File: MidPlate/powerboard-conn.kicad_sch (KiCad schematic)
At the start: 10 parts, among them J3 Molex Microfit 3.0

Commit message: update to midplate
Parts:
- removed J3 (x2): Molex Microfit 3.0, bots:Molex_Micro-Fit_3.0_43650-0215_1x02_P3.00mm_Vertical, symbol bots:Molex_Microfit_3.0_1x2
- added J4, J5: Molex MicroFit 1x2_SMD, bots:Molex_Micro-Fit_3.0_43650-0224_1x02-1MP_P3.00mm_Vertical, symbol bots:Molex_Microfit_3.0_1x2_SMD
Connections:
- net CHICKER: now also J4.2 (Pin_2)
- net EXTRA: now also J5.2 (Pin_2)
- net HV: now also J4.1 (Pin_1), J5.1 (Pin_1)

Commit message: midplate mods
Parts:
- removed H1: VCC_PB, bots:MountingHole_2.7mm_M2.5_DIN965_Pad, symbol Mechanical:MountingHole_Pad
- removed H2: GND_PB, bots:MountingHole_2.7mm_M2.5_DIN965_Pad, symbol Mechanical:MountingHole_Pad
- removed H3: CANL_PB, bots:MountingHole_2.7mm_M2.5_DIN965_Pad, symbol Mechanical:MountingHole_Pad
- removed H4: CANH_PB, bots:MountingHole_2.7mm_M2.5_DIN965_Pad, symbol Mechanical:MountingHole_Pad
- removed H5: NC, bots:MountingHole_2.7mm_M2.5_DIN965_Pad, symbol Mechanical:MountingHole_Pad
- removed H6: EXTRA, bots:MountingHole_2.7mm_M2.5_DIN965_Pad, symbol Mechanical:MountingHole_Pad
- removed H7: HV, bots:MountingHole_2.7mm_M2.5_DIN965_Pad, symbol Mechanical:MountingHole_Pad
- removed H8: CHICKER, bots:MountingHole_2.7mm_M2.5_DIN965_Pad, symbol Mechanical:MountingHole_Pad
- added H1: VCC_PB, bots:Keystone_24929, symbol bots:ZeroH_Keystone24929_Pad
- added H2: GND_PB, bots:Keystone_24929, symbol bots:ZeroH_Keystone24929_Pad
- added H3: CANL_PB, bots:Keystone_24929, symbol bots:ZeroH_Keystone24929_Pad
- added H4: CANH_PB, bots:Keystone_24929, symbol bots:ZeroH_Keystone24929_Pad
- added H5: NC, bots:Keystone_24929, symbol bots:ZeroH_Keystone24929_Pad
- added H6: EXTRA, bots:Keystone_24929, symbol bots:ZeroH_Keystone24929_Pad
- added H7: HV, bots:Keystone_24929, symbol bots:ZeroH_Keystone24929_Pad
- added H8: CHICKER, bots:Keystone_24929, symbol bots:ZeroH_Keystone24929_Pad
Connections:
- net CHICKER: now also H8.1
- net EXTRA: now also H6.1
- net GND: now also H2.1
- net HV: now also H7.1
- net VCC: now also H1.1
- new net CAN+: H4.1
- new net CAN-: H3.1
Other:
- moved on the sheet: J4, J5

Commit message: midplate changes, ready for order
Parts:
- added J13: JST_BM04B-GHS-TBT, bots:JST_BM04B-GHS-TBT, symbol bots:JST_BM04B-GHS-TBT
- added R4, R5: R_0OHM_JUMPER, bots:R_0603_1608Metric, symbol bots:R_0OHM_JUMPER
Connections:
- net CAN+: now also J13.3, R4.1; no longer H4.1
- net CAN-: now also J13.2, R5.2; no longer H3.1
- net GND: now also J13.1, J13.4
- new net CANR+: H4.1, R4.2
- new net CANR-: H3.1, R5.1
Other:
- moved on the sheet: H3, H4

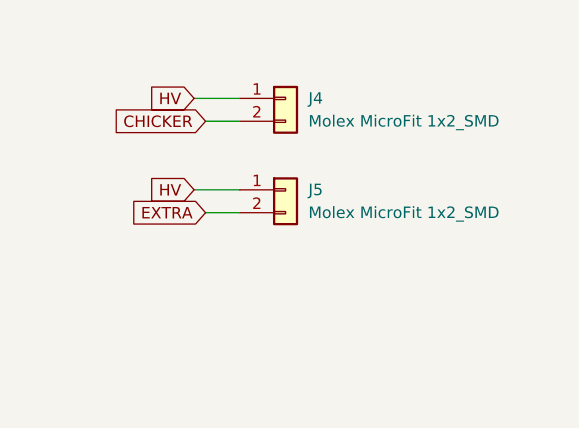
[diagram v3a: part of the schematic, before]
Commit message: midplate updates
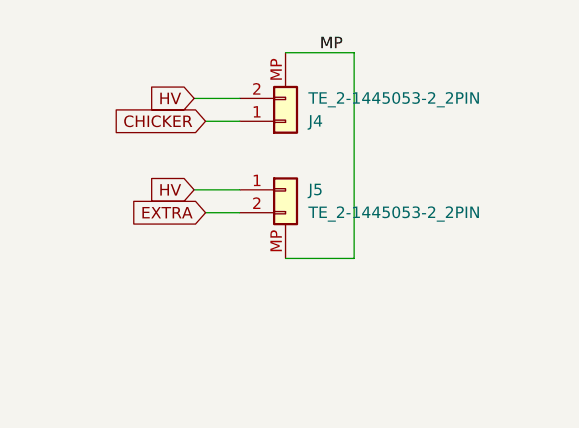
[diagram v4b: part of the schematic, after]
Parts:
- removed J4, J5: Molex MicroFit 1x2_SMD, bots:Molex_Micro-Fit_3.0_43650-0224_1x02-1MP_P3.00mm_Vertical, symbol bots:Molex_Microfit_3.0_1x2_SMD
- added J4, J5: TE_2-1445053-2_2PIN, bots:TE_2-1445053-2_2PIN, symbol bots:TE_2-1445053-2_2PIN
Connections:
- net CHICKER: now also J4.1 (Pin_1)
- net EXTRA: now also J5.2 (Pin_2)
- net HV: now also J4.2 (Pin_2), J5.1 (Pin_1)
- new net MP: J4.MP, J4.MP1, J5.MP, J5.MP1

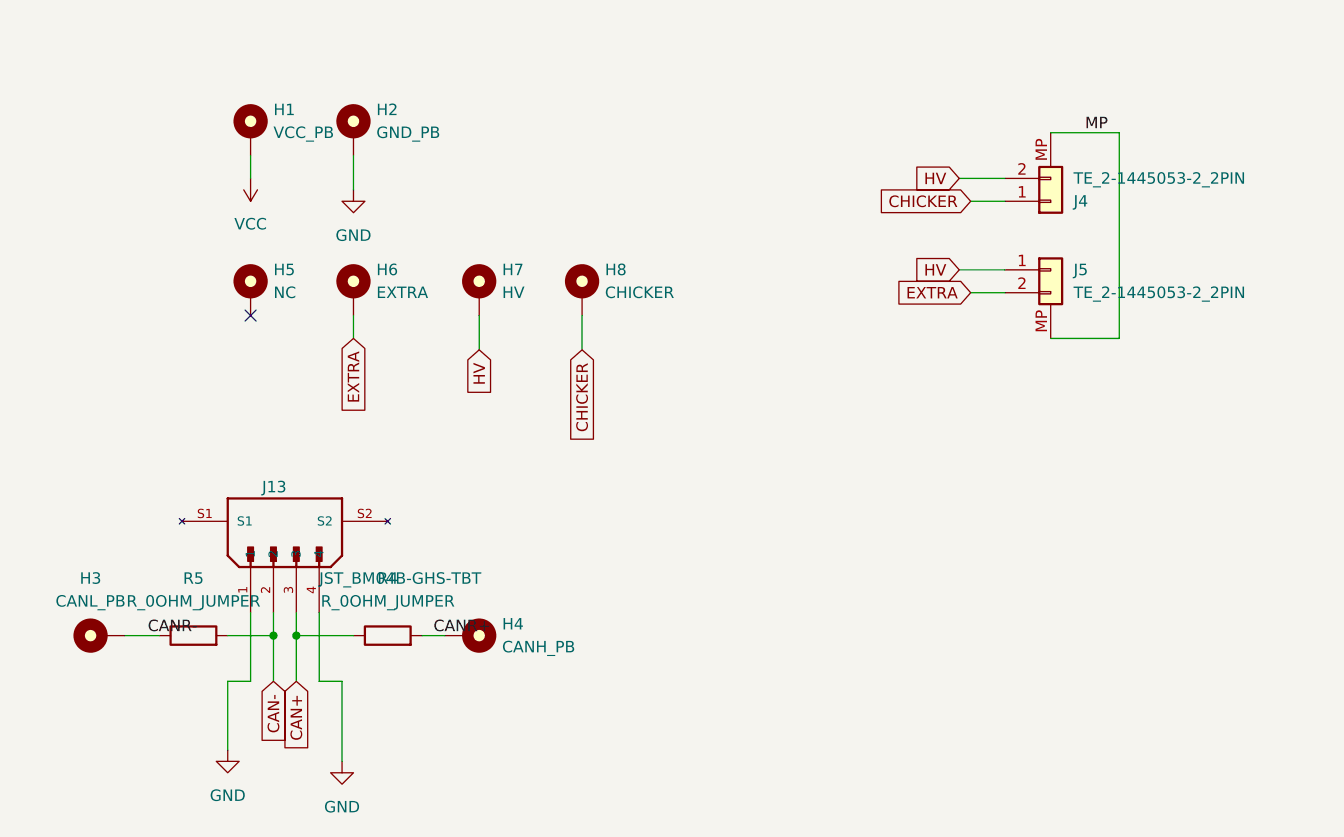
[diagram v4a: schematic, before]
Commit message: midplate 5V buck converter
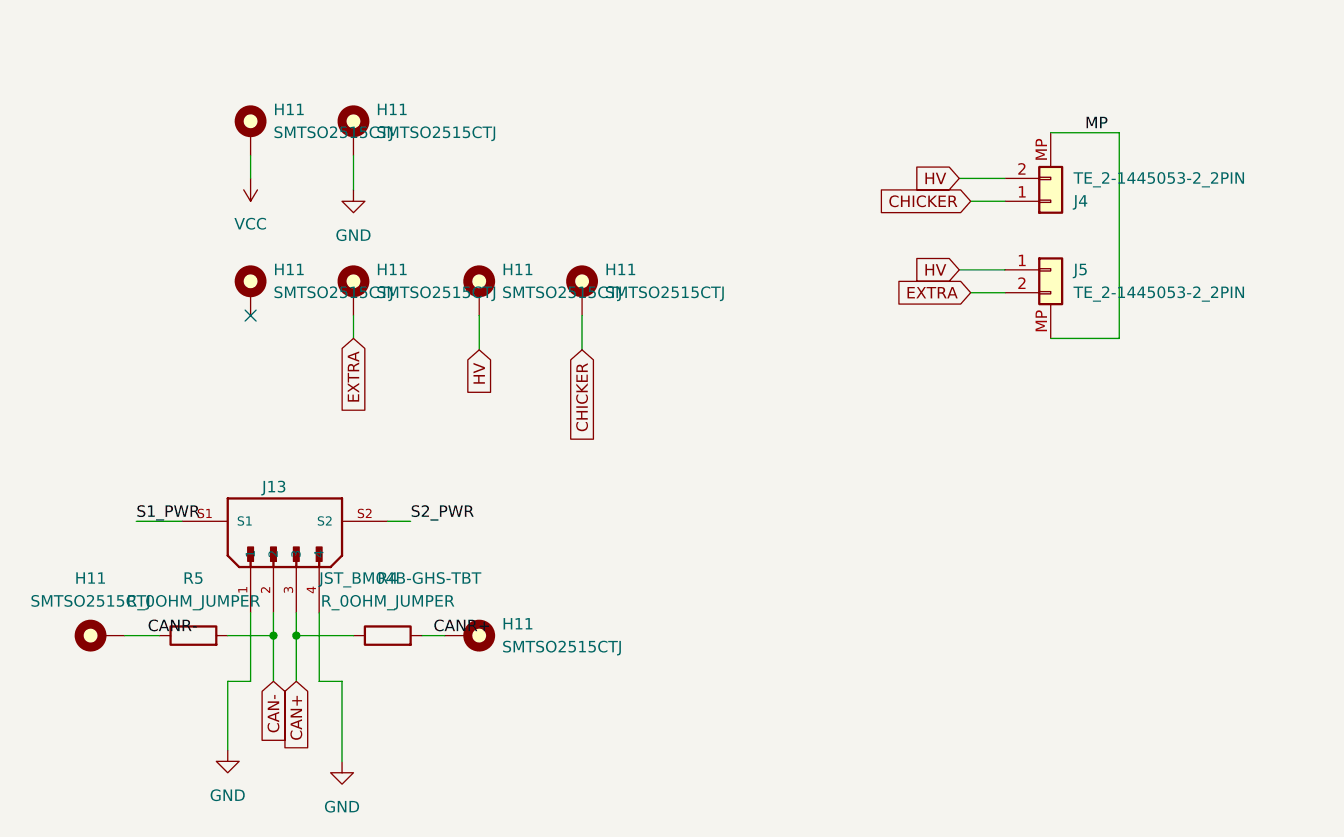
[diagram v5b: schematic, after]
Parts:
- removed H1: VCC_PB, bots:Keystone_24929, symbol bots:ZeroH_Keystone24929_Pad
- removed H2: GND_PB, bots:Keystone_24929, symbol bots:ZeroH_Keystone24929_Pad
- removed H3: CANL_PB, bots:Keystone_24929, symbol bots:ZeroH_Keystone24929_Pad
- removed H4: CANH_PB, bots:Keystone_24929, symbol bots:ZeroH_Keystone24929_Pad
- removed H5: NC, bots:Keystone_24929, symbol bots:ZeroH_Keystone24929_Pad
- removed H6: EXTRA, bots:Keystone_24929, symbol bots:ZeroH_Keystone24929_Pad
- removed H7: HV, bots:Keystone_24929, symbol bots:ZeroH_Keystone24929_Pad
- removed H8: CHICKER, bots:Keystone_24929, symbol bots:ZeroH_Keystone24929_Pad
- added H11 (x8): SMTSO2515CTJ, bots:SMTSO2515CTJ, symbol bots:SMTSO2515CTJ
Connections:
- net CANR+: now also H11.1
- net CANR-: now also H11.1
- net CHICKER: now also H11.1
- net EXTRA: now also H11.1
- net GND: now also H11.1
- net HV: now also H11.1
- net VCC: now also H11.1
- net S1_PWR: now reaches J13.S1
- net S2_PWR: now reaches J13.S2

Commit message: midplate v1 ready for review
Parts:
- J13: now not fitted; now left out of the parts list
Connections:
- net +5V: now reaches H11.1
- no-connect marks 1 -> 0
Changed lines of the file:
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@@
   (junction (at 49.53 99.06) (diameter 0) (color 0 0 0 0)
   )
-  (no_connect (at 46.99 63.5))
   (wire (pts (xy 72.39 63.5) (xy 72.39 67.31))
     (stroke (width 0) (type default))
@@
     (property "Intersheetrefs" "${INTERSHEET_REFS}" (at 120.3257 48.26 0)
       (effects (font (size 1.27 1.27)) (justify right) hide)
+    )
+  )
+  (symbol (lib_id "power:+5V") (at 46.99 63.5 180) (unit 1)
+    (in_bom yes) (on_board yes) (dnp no)
+    (property "Reference" "#PWR013" (at 46.99 59.69 0)
+      (effects (font (size 1.27 1.27)) hide)
+    )
+    (property "Value" "+5V" (at 46.99 67.31 0)
+      (effects (font (size 1.27 1.27)))
+    )
+    (property "Footprint" "" (at 46.99 63.5 0)
+      (effects (font (size 1.27 1.27)) hide)
+    )
+    (property "Datasheet" "" (at 46.99 63.5 0)
+      (effects (font (size 1.27 1.27)) hide)
+    )
+    (pin "1")
+    (instances
+      (project "midplate"
+        (path "/69058343-dac8-421b-a3f6-e069eb1ba8ae/ab54f000-c596-4ae0-81be-92723dd47fdf"
+          (reference "#PWR013") (unit 1)
+        )
+        (path "/69058343-dac8-421b-a3f6-e069eb1ba8ae/5699b499-0901-4542-927f-3a0270375bb5"
+          (reference "#PWR020") (unit 1)
+        )
+      )
+      (project "FacePlate"
+        (path "/e63e39d7-6ac0-4ffd-8aa3-1841a4541b55"
+          (reference "#PWR043") (unit 1)
+        )
+      )
     )
   )
@@
   )
   (symbol (lib_id "bots:JST_BM04B-GHS-TBT") (at 49.53 91.44 90) (unit 1)
-    (in_bom yes) (on_board yes) (dnp no)
+    (in_bom no) (on_board yes) (dnp yes)
     (property "Reference" "J13" (at 48.26 82.55 90)
       (effects (font (size 1.27 1.27)) (justify right))

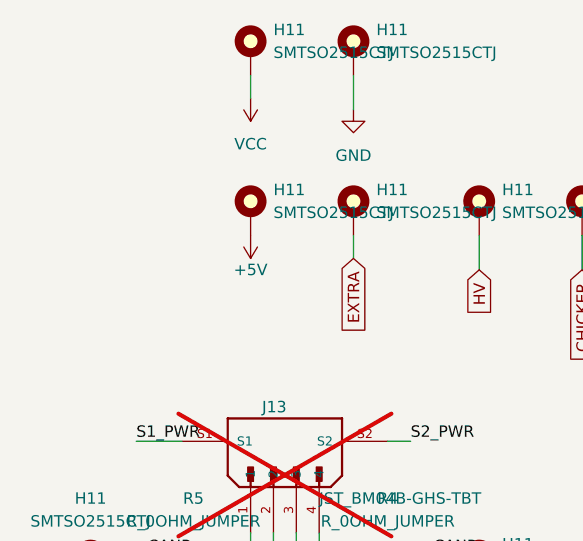
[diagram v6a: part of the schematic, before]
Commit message: power board and midplate updates (mostly finalized)
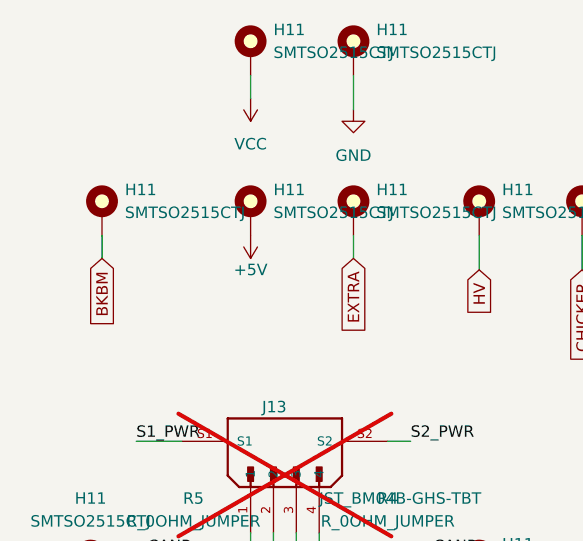
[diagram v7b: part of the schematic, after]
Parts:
- added H11: SMTSO2515CTJ, bots:SMTSO2515CTJ, symbol bots:SMTSO2515CTJ
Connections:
- new net BKBM: H11.1
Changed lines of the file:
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@@
+    (stroke (width 0) (type default))
+  )
+  (wire (pts (xy 30.48 63.5) (xy 30.48 66.04))
     (stroke (width 0) (type default))
   )
@@
     )
   )
+  (global_label "BKBM" (shape input) (at 30.48 66.04 270) (fields_autoplaced)
+    (effects (font (size 1.27 1.27)) (justify right))
+    (property "Intersheetrefs" "${INTERSHEET_REFS}" (at 30.48 74.2866 90)
+      (effects (font (size 1.27 1.27)) (justify right) hide)
+    )
+  )
+  (symbol (lib_id "bots:SMTSO2515CTJ") (at 30.48 60.96 0) (unit 1)
+    (in_bom yes) (on_board yes) (dnp no) (fields_autoplaced)
+    (property "Reference" "H11" (at 33.02 58.42 0)
+      (effects (font (size 1.27 1.27)) (justify left))
+    )
+    (property "Value" "SMTSO2515CTJ" (at 33.02 60.96 0)
+      (effects (font (size 1.27 1.27)) (justify left))
+    )
+    (property "Footprint" "bots:SMTSO2515CTJ" (at 30.48 60.96 0)
+      (effects (font (size 1.27 1.27)) hide)
+    )
+    (property "Datasheet" "~" (at 30.48 60.96 0)
+      (effects (font (size 1.27 1.27)) hide)
+    )
+    (pin "1")
+    (instances
+      (project "midplate"
+        (path "/69058343-dac8-421b-a3f6-e069eb1ba8ae/dd4f1e83-2671-4cd9-8990-217fc355ed24"
+          (reference "H11") (unit 1)
+        )
+        (path "/69058343-dac8-421b-a3f6-e069eb1ba8ae/5699b499-0901-4542-927f-3a0270375bb5"
+          (reference "H9") (unit 1)
+        )
+      )
+    )
+  )

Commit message: midplate
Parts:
- H11: value SMTSO2515CTJ -> BKBM
- H11: value SMTSO2515CTJ -> CANH
- H11: value SMTSO2515CTJ -> HV
- H11: value SMTSO2515CTJ -> GND
- H11: value SMTSO2515CTJ -> EXTRA
- H11: value SMTSO2515CTJ -> VCC
- H11: value SMTSO2515CTJ -> CHICKER
- H11: value SMTSO2515CTJ -> 5V
- H11: value SMTSO2515CTJ -> CANL
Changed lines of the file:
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@@
       (effects (font (size 1.27 1.27)) (justify left))
     )
-    (property "Value" "SMTSO2515CTJ" (at 33.02 60.96 0)
+    (property "Value" "BKBM" (at 33.02 60.96 0)
       (effects (font (size 1.27 1.27)) (justify left))
     )
@@
       (effects (font (size 1.27 1.27)) (justify left))
     )
-    (property "Value" "SMTSO2515CTJ" (at 74.93 100.33 90)
+    (property "Value" "CANH" (at 74.93 100.33 90)
       (effects (font (size 1.27 1.27)) (justify left))
     )
@@
       (effects (font (size 1.27 1.27)) (justify left))
     )
-    (property "Value" "SMTSO2515CTJ" (at 74.93 60.96 0)
+    (property "Value" "HV" (at 74.93 60.96 0)
       (effects (font (size 1.27 1.27)) (justify left))
     )
@@
       (effects (font (size 1.27 1.27)) (justify left))
     )
-    (property "Value" "SMTSO2515CTJ" (at 60.96 43.18 0)
+    (property "Value" "GND" (at 60.96 43.18 0)
       (effects (font (size 1.27 1.27)) (justify left))
     )
@@
       (effects (font (size 1.27 1.27)) (justify left))
     )
-    (property "Value" "SMTSO2515CTJ" (at 60.96 60.96 0)
+    (property "Value" "EXTRA" (at 60.96 60.96 0)
       (effects (font (size 1.27 1.27)) (justify left))
     )
@@
       (effects (font (size 1.27 1.27)) (justify left))
     )
-    (property "Value" "SMTSO2515CTJ" (at 49.53 43.18 0)
+    (property "Value" "VCC" (at 49.53 43.18 0)
       (effects (font (size 1.27 1.27)) (justify left))
     )
@@
       (effects (font (size 1.27 1.27)) (justify left))
     )
-    (property "Value" "SMTSO2515CTJ" (at 86.36 60.96 0)
+    (property "Value" "CHICKER" (at 86.36 60.96 0)
       (effects (font (size 1.27 1.27)) (justify left))
     )
@@
       (effects (font (size 1.27 1.27)) (justify left))
     )
-    (property "Value" "SMTSO2515CTJ" (at 49.53 60.96 0)
+    (property "Value" "5V" (at 49.53 60.96 0)
       (effects (font (size 1.27 1.27)) (justify left))
     )
@@
       (effects (font (size 1.27 1.27)))
     )
-    (property "Value" "SMTSO2515CTJ" (at 29.21 95.25 90)
-      (effects (font (size 1.27 1.27)))
-    )
+    (property "Value" "CANL" (at 29.21 95.25 90)
+      (effects (font (size 1.27 1.27)))
+    )
